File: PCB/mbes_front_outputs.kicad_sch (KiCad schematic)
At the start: 72 parts, among them IC2 BDX34C, IC3 BDX34C, K1 RT42xxxx, Q1 D45VH10, Q10 BC337, Q11 BC337, Q12 BC327, Q13 BC337, Q14 D45VH10, Q15 D45VH10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

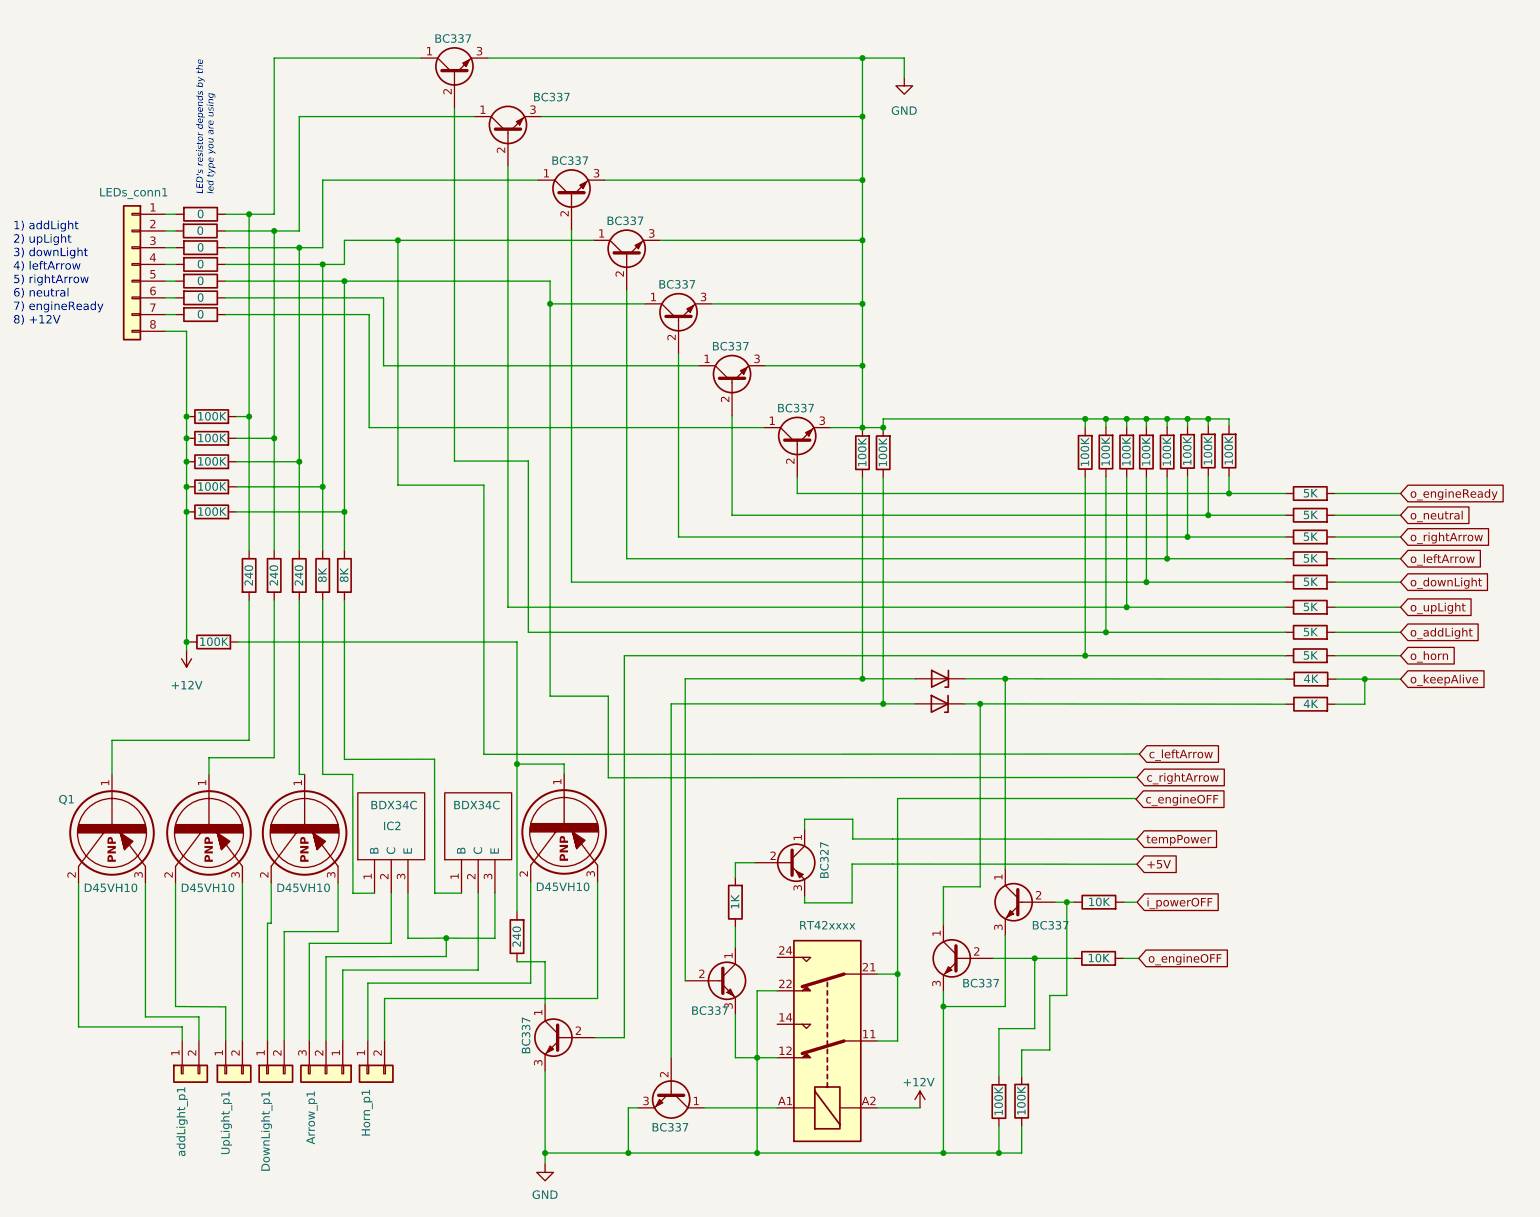
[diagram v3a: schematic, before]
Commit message: External cockpit power-connector added and wrong transistor type fixed
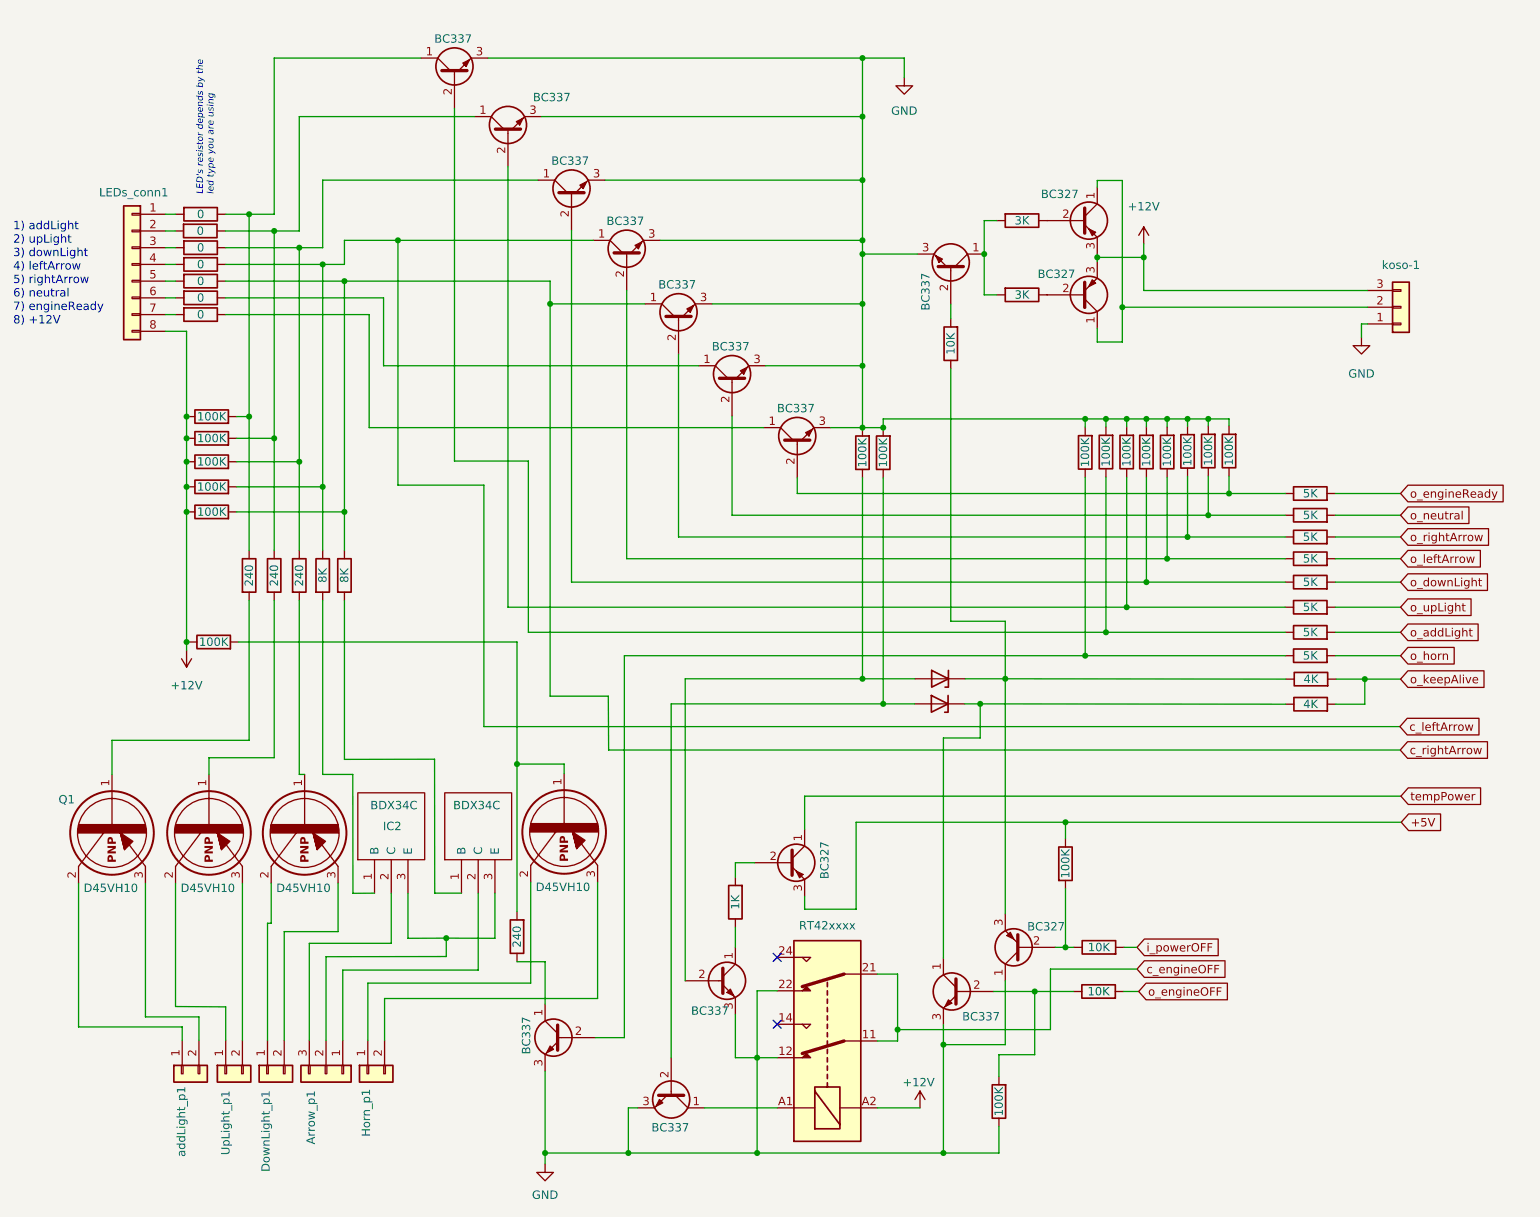
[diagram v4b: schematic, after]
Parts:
- added Q18, Q19, Q20: BC327, Package_TO_SOT_THT:TO-92L_Inline_Wide, symbol Transistor_BJT:BC327
- added RA45: 10K, Resistor_THT:R_Axial_DIN0207_L6.3mm_D2.5mm_P7.62mm_Horizontal, symbol Device:R
- added RA46, RA47: 3K, Resistor_THT:R_Axial_DIN0207_L6.3mm_D2.5mm_P7.62mm_Horizontal, symbol Device:R
- added koso-1: Conn_01x03, Connector_PinHeader_2.54mm:PinHeader_1x03_P2.54mm_Vertical, symbol Connector_Generic:Conn_01x03
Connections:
- net +12V: now also Q19.3 (E), Q20.3 (E), koso-1.3 (Pin_3)
- net +5V: now also RA44.1
- net GND: now also Q18.1 (C), koso-1.1 (Pin_1); no longer RA44.1
- net at D4.1 (K), RA8.1: now also Q18.3 (E), RA45.1; no longer Q16.1 (C)
- net at RA29.1, RA44.2: now also Q18.2 (B); no longer Q16.2 (B)
- new net: Q19.2 (B), RA46.1
- new net: Q16.1 (C), RA46.2, RA47.2
- new net: Q19.1 (C), Q20.1 (C), koso-1.2 (Pin_2)
- new net: Q16.2 (B), RA45.2
- new net: Q20.2 (B), RA47.1
- no-connect marks 0 -> 2

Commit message: Fixes and optimizations (unuseful I/O lines dropped)
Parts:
- added RA48, RA49: 100K, Resistor_THT:R_Axial_DIN0207_L6.3mm_D2.5mm_P7.62mm_Horizontal, symbol Device:R
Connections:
- net +12V: now also RA49.2
- net GND: now also RA48.2
- net at Q16.1 (C), RA46.2, RA47.2: now also RA49.1
- net at D4.1 (K), Q18.3 (E), RA45.1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: now also RA48.1
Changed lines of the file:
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@@
 (kicad_sch (version 20211123) (generator eeschema)
   (paper "A4")
+  (junction (at 164.6428 45.3136) (diameter 0) (color 0 0 0 0)
+  )
   (junction (at 158.4452 186.944) (diameter 0) (color 0 0 0 0)
   )
@@
   (junction (at 192.4304 96.6724) (diameter 0) (color 0 0 0 0)
   )
+  (junction (at 188.8744 34.5948) (diameter 0) (color 0 0 0 0)
+  )
   (junction (at 146.1516 57.9628) (diameter 0) (color 0 0 0 0)
   )
@@
   )
   (junction (at 146.1516 20.6248) (diameter 0) (color 0 0 0 0)
+  )
+  (junction (at 159.5628 70.7136) (diameter 0) (color 0 0 0 0)
+  )
+  (junction (at 146.1516 70.7136) (diameter 0) (color 0 0 0 0)
   )
   (junction (at 67.4624 54.5084) (diameter 0) (color 0 0 0 0)
@@
     (stroke (width 0) (type default) (color 0 0 0 0))
   )
+  (wire (pts (xy 146.1516 70.7136) (xy 146.1516 76.7588))
+    (stroke (width 0) (type default) (color 0 0 0 0))
+  )
   (wire (pts (xy 167.8432 170.4848) (xy 167.8432 160.782))
     (stroke (width 0) (type default) (color 0 0 0 0))
   )
+  (wire (pts (xy 164.6428 43.8912) (xy 164.6428 45.3136))
+    (stroke (width 0) (type default) (color 0 0 0 0))
+  )
   (wire (pts (xy 40.2844 59.5884) (xy 41.8084 59.5884))
     (stroke (width 0) (type default) (color 0 0 0 0))
@@
     (stroke (width 0) (type default) (color 0 0 0 0))
   )
+  (wire (pts (xy 188.8744 34.5948) (xy 164.6428 34.5948))
+    (stroke (width 0) (type default) (color 0 0 0 0))
+  )
   (wire (pts (xy 40.2844 54.5084) (xy 41.8084 54.5084))
     (stroke (width 0) (type default) (color 0 0 0 0))
@@
     (stroke (width 0) (type default) (color 0 0 0 0))
   )
+  (wire (pts (xy 156.3116 70.7136) (xy 159.5628 70.7136))
+    (stroke (width 0) (type default) (color 0 0 0 0))
+  )
   (wire (pts (xy 222.4532 118.7704) (xy 222.4532 114.9604))
     (stroke (width 0) (type default) (color 0 0 0 0))
@@
     (stroke (width 0) (type default) (color 0 0 0 0))
   )
-  (wire (pts (xy 188.8744 48.8188) (xy 188.8744 50.9016))
+  (wire (pts (xy 188.8744 34.5948) (xy 188.8744 50.9016))
     (stroke (width 0) (type default) (color 0 0 0 0))
   )
@@
     (stroke (width 0) (type default) (color 0 0 0 0))
   )
+  (wire (pts (xy 164.6428 34.5948) (xy 164.6428 36.2712))
+    (stroke (width 0) (type default) (color 0 0 0 0))
+  )
   (wire (pts (xy 167.8432 114.9096) (xy 167.8432 150.622))
     (stroke (width 0) (type default) (color 0 0 0 0))
@@
     (stroke (width 0) (type default) (color 0 0 0 0))
   )
+  (wire (pts (xy 159.5628 70.7136) (xy 159.5628 106.172))
+    (stroke (width 0) (type default) (color 0 0 0 0))
+  )
   (wire (pts (xy 93.6752 109.3216) (xy 93.6752 127.8636))
     (stroke (width 0) (type default) (color 0 0 0 0))
@@
     (stroke (width 0) (type default) (color 0 0 0 0))
   )
-  (wire (pts (xy 159.5628 67.818) (xy 159.5628 106.172))
+  (wire (pts (xy 159.5628 67.818) (xy 159.5628 70.7136))
     (stroke (width 0) (type default) (color 0 0 0 0))
   )
@@
     (stroke (width 0) (type default) (color 0 0 0 0))
   )
-  (wire (pts (xy 146.1516 67.3608) (xy 146.1516 76.7588))
+  (wire (pts (xy 146.1516 67.3608) (xy 146.1516 70.7136))
     (stroke (width 0) (type default) (color 0 0 0 0))
   )
@@
   )
   (wire (pts (xy 192.4304 75.438) (xy 192.4304 76.6572))
+    (stroke (width 0) (type default) (color 0 0 0 0))
+  )
+  (wire (pts (xy 146.1516 70.7136) (xy 148.6916 70.7136))
     (stroke (width 0) (type default) (color 0 0 0 0))
   )
@@
     )
     (property "Datasheet" "~" (id 3) (at 64.1604 99.2124 0)
+      (effects (font (size 1.27 1.27)) hide)
+    )
+    (pin "1")
+    (pin "2")
+  )
+  (symbol (lib_id "Device:R") (at 164.6428 40.0812 180) (unit 1)
+    (in_bom yes) (on_board yes)
+    (property "Reference" "RA49" (id 0) (at 170.9928 40.0812 90)
+      (effects (font (size 1.27 1.27)) hide)
+    )
+    (property "Value" "100K" (id 1) (at 164.6428 40.0812 90))
+    (property "Footprint" "Resistor_THT:R_Axial_DIN0207_L6.3mm_D2.5mm_P7.62mm_Horizontal" (id 2) (at 166.4208 40.0812 90)
+      (effects (font (size 1.27 1.27)) hide)
+    )
+    (property "Datasheet" "~" (id 3) (at 164.6428 40.0812 0)
       (effects (font (size 1.27 1.27)) hide)
     )
@@
     (pin "2")
   )
+  (symbol (lib_id "Device:R") (at 152.5016 70.7136 270) (unit 1)
+    (in_bom yes) (on_board yes)
+    (property "Reference" "RA48" (id 0) (at 152.5016 64.3636 90)
+      (effects (font (size 1.27 1.27)) hide)
+    )
+    (property "Value" "100K" (id 1) (at 152.5016 70.7136 90))
+    (property "Footprint" "Resistor_THT:R_Axial_DIN0207_L6.3mm_D2.5mm_P7.62mm_Horizontal" (id 2) (at 152.5016 68.9356 90)
+      (effects (font (size 1.27 1.27)) hide)
+    )
+    (property "Datasheet" "~" (id 3) (at 152.5016 70.7136 0)
+      (effects (font (size 1.27 1.27)) hide)
+    )
+    (pin "1")
+    (pin "2")
+  )
   (symbol (lib_id "Device:R") (at 126.8476 148.844 180) (unit 1)
     (in_bom yes) (on_board yes)
@@
     (pin "2")
   )
-  (symbol (lib_id "power:+12V") (at 188.8744 48.8188 0) (unit 1)
+  (symbol (lib_id "power:+12V") (at 188.8744 34.5948 0) (unit 1)
     (in_bom yes) (on_board yes) (fields_autoplaced)
-    (property "Reference" "#PWR0110" (id 0) (at 188.8744 52.6288 0)
-      (effects (font (size 1.27 1.27)) hide)
-    )
-    (property "Value" "+12V" (id 1) (at 188.8744 43.18 0))
-    (property "Footprint" "" (id 2) (at 188.8744 48.8188 0)
-      (effects (font (size 1.27 1.27)) hide)
-    )
-    (property "Datasheet" "" (id 3) (at 188.8744 48.8188 0)
-      (effects (font (size 1.27 1.27)) hide)
-    )
+    (property "Reference" "#PWR0110" (id 0) (at 188.8744 38.4048 0)
+      (effects (font (size 1.27 1.27)) hide)
+    )
+    (property "Value" "+12V" (id 1) (at 188.8744 28.956 0))
+    (property "Footprint" "" (id 2) (at 188.8744 34.5948 0)
+      (effects (font (size 1.27 1.27)) hide)
+    )
+    (property "Datasheet" "" (id 3) (at 188.8744 34.5948 0)
+      (effects (font (size 1.27 1.27)) hide)
+    )

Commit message: fixes
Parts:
- removed D3, D4: 2V, Diode_THT:D_DO-35_SOD27_P7.62mm_Horizontal, symbol Diode:BZD27Cxx
- removed K1: RT42xxxx, Relay_THT:Relay_DPDT_Schrack-RT2-FormC_RM5mm, symbol Relay:RT42xxxx
- removed Q11, Q13, Q16, Q17: BC337, Package_TO_SOT_THT:TO-92L_Inline_Wide, symbol Transistor_BJT:BC337
- removed Q12, Q18, Q19, Q20: BC327, Package_TO_SOT_THT:TO-92L_Inline_Wide, symbol Transistor_BJT:BC327
- removed RA23: 5K, Resistor_THT:R_Axial_DIN0207_L6.3mm_D2.5mm_P7.62mm_Horizontal, symbol Device:R
- removed RA29, RA33, RA45: 10K, Resistor_THT:R_Axial_DIN0207_L6.3mm_D2.5mm_P7.62mm_Horizontal, symbol Device:R
- removed RA30, RA31, RA43, RA44, RA48, RA49: 100K, Resistor_THT:R_Axial_DIN0207_L6.3mm_D2.5mm_P7.62mm_Horizontal, symbol Device:R
- removed RA41, RA8: 4K, Resistor_THT:R_Axial_DIN0207_L6.3mm_D2.5mm_P7.62mm_Horizontal, symbol Device:R
- removed RA46, RA47: 3K, Resistor_THT:R_Axial_DIN0207_L6.3mm_D2.5mm_P7.62mm_Horizontal, symbol Device:R
- removed RA7: 1K, Resistor_THT:R_Axial_DIN0207_L6.3mm_D2.5mm_P7.62mm_Horizontal, symbol Device:R
- removed koso-1: Conn_01x03, Connector_PinHeader_2.54mm:PinHeader_1x03_P2.54mm_Vertical, symbol Connector_Generic:Conn_01x03
- added RA?: 5K, Resistor_THT:R_Axial_DIN0207_L6.3mm_D2.5mm_P7.62mm_Horizontal, symbol Device:R
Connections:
- net o_horn: now also RA?.2
- net at Q9.2 (B), RA32.1: now also RA?.1
- no-connect marks 2 -> 0

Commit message: fixes
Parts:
- RA15: footprint Resistor_THT:R_Axial_DIN0207_L6.3mm_D2.5mm_P7.62mm_Horizontal -> Resistor_THT:R_Axial_DIN0414_L11.9mm_D4.5mm_P15.24mm_Horizontal
- gave numbers to parts that had none: 1
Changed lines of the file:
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@@
     )
     (property "Value" "240" (id 1) (at 93.6752 116.9416 90))
-    (property "Footprint" "Resistor_THT:R_Axial_DIN0207_L6.3mm_D2.5mm_P7.62mm_Horizontal" (id 2) (at 95.4532 116.9416 90)
+    (property "Footprint" "Resistor_THT:R_Axial_DIN0414_L11.9mm_D4.5mm_P15.24mm_Horizontal" (id 2) (at 95.4532 116.9416 90)
       (effects (font (size 1.27 1.27)) hide)
     )
@@
   (symbol (lib_id "Device:R") (at 214.1728 111.4044 90) (unit 1)
     (in_bom yes) (on_board yes)
-    (property "Reference" "RA?" (id 0) (at 214.1728 117.7544 90)
-      (effects (font (size 1.27 1.27)) hide)
-    )
+    (property "Reference" "RA7" (id 0) (at 214.1728 117.7544 90)
+      (effects (font (size 1.27 1.27)) hide)
+    )
